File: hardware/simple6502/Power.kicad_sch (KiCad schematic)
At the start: 23 parts, among them J5 POWER 5V, J6 AUX 5VDC, SW2 POWER, U5 74HCT00, U6 74LS30, U7 74HCT273

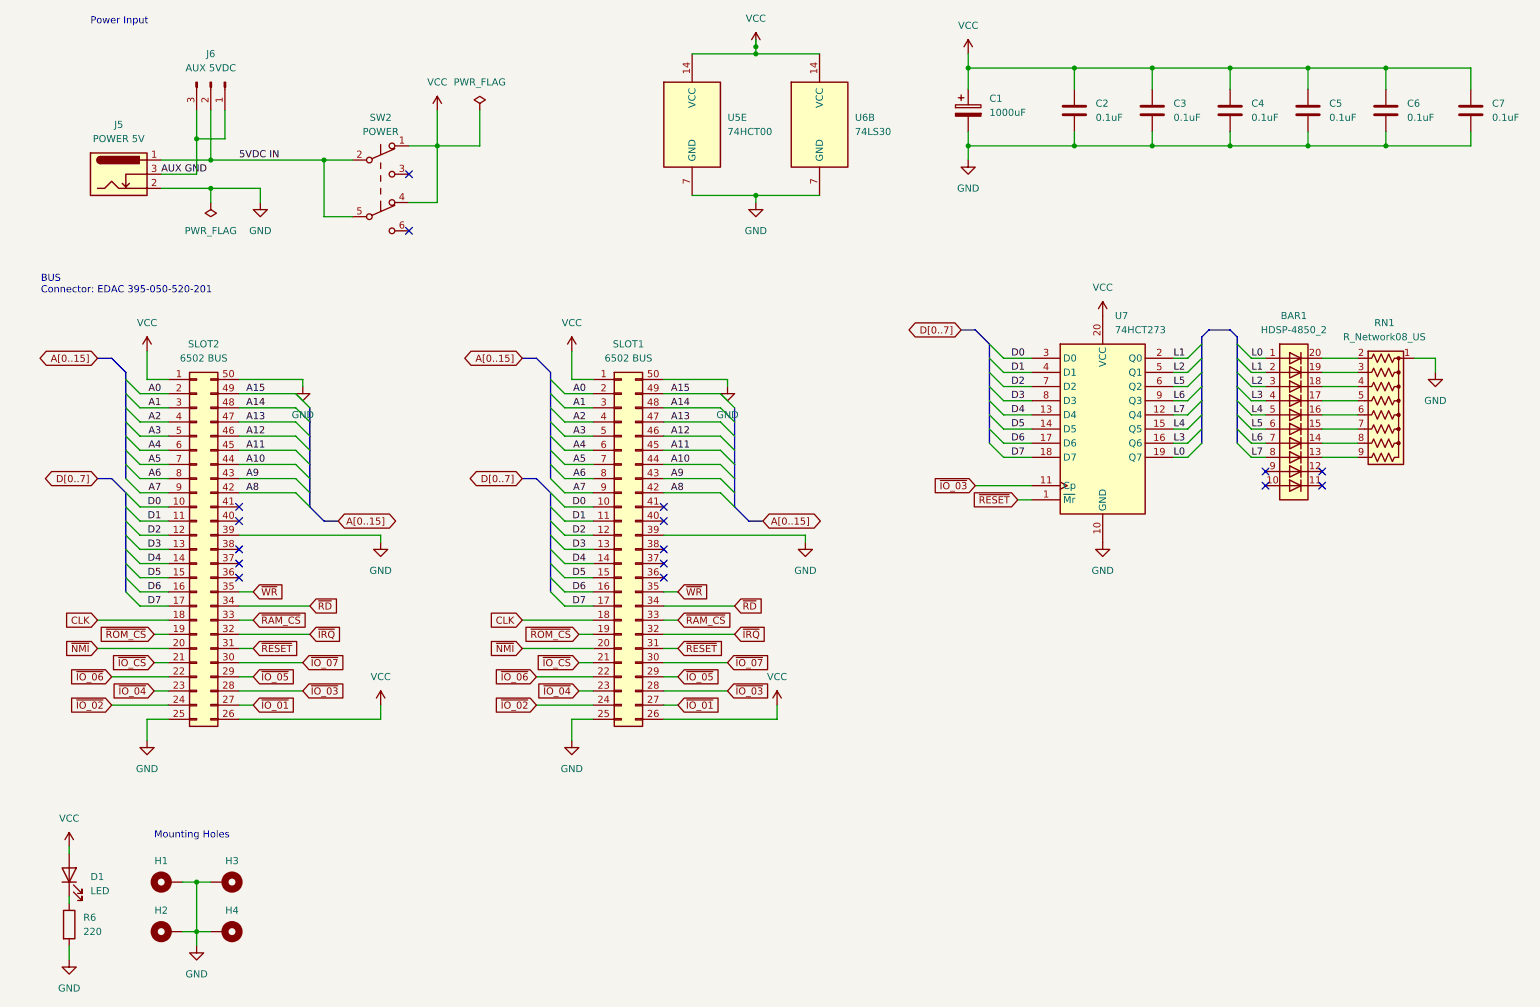
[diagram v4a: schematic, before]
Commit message: adding Debug leds in IO_8
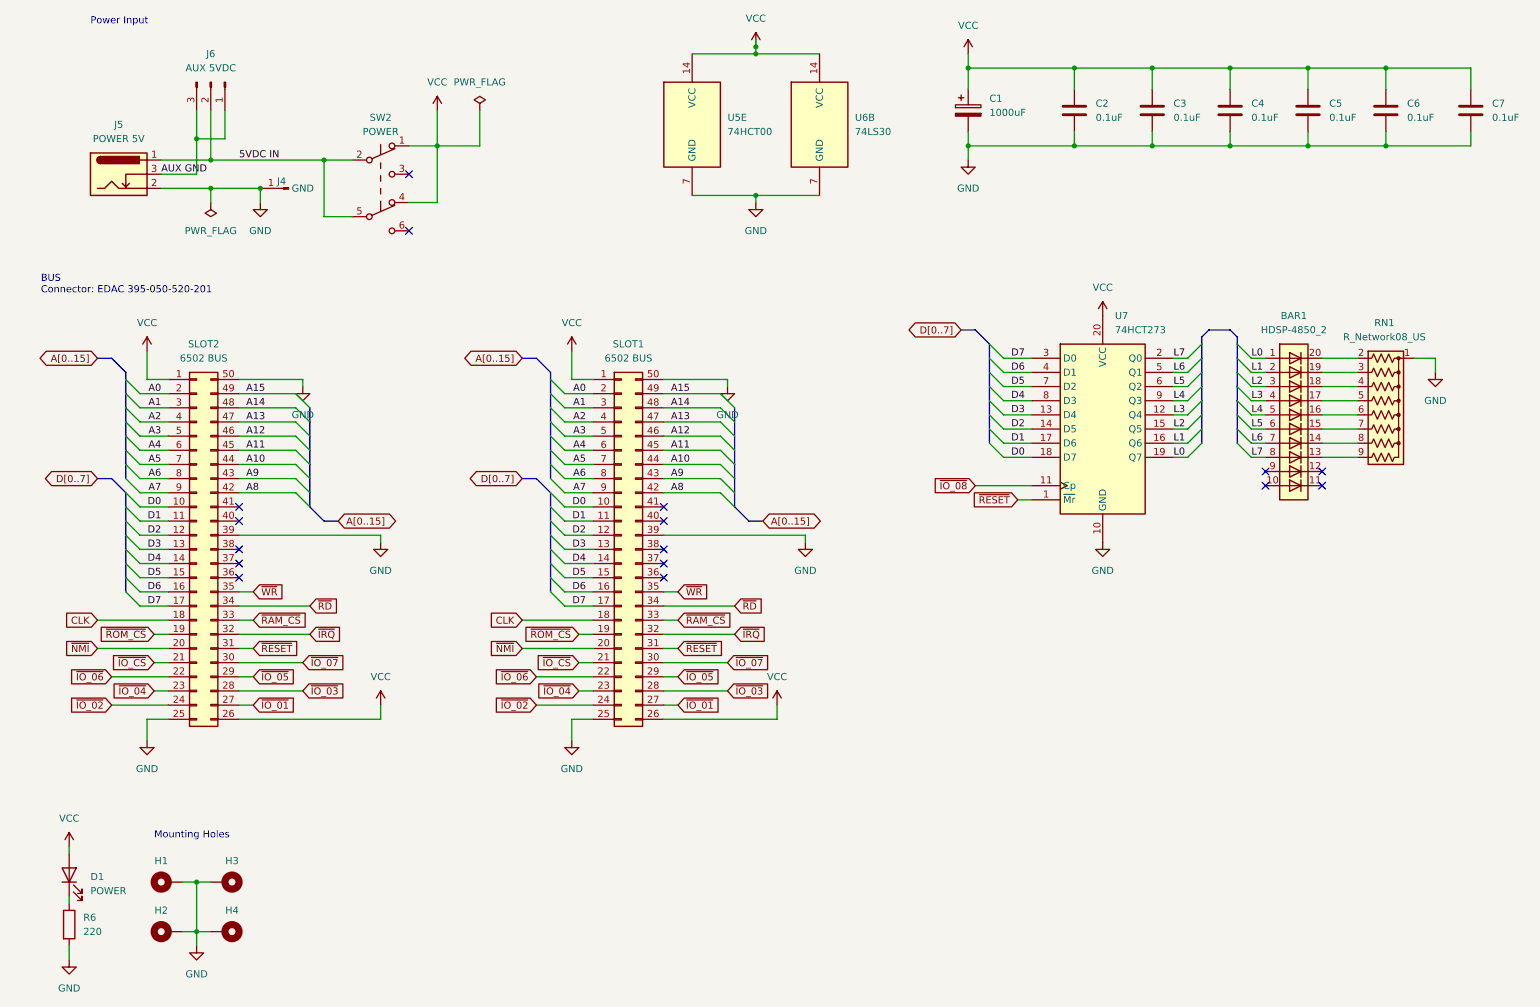
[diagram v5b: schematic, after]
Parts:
- added J4: GND, Connector_PinHeader_2.54mm:PinHeader_1x01_P2.54mm_Vertical, symbol Connector:Conn_01x01_Pin
- D1: value LED -> POWER
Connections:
- net D0: now also U7.18 (D7); no longer U7.3 (D0)
- net D1: now also U7.17 (D6); no longer U7.4 (D1)
- net D2: now also U7.14 (D5); no longer U7.7 (D2)
- net D3: now also U7.13 (D4); no longer U7.8 (D3)
- net D4: now also U7.8 (D3); no longer U7.13 (D4)
- net D5: now also U7.7 (D2); no longer U7.14 (D5)
- net D6: now also U7.4 (D1); no longer U7.17 (D6)
- net D7: now also U7.3 (D0); no longer U7.18 (D7)
- net GND: now also J4.1 (Pin_1)
- net L1: now also U7.16 (Q6); no longer U7.2 (Q0)
- net L2: now also U7.15 (Q5); no longer U7.5 (Q1)
- net L3: now also U7.12 (Q4); no longer U7.16 (Q6)
- net L4: now also U7.9 (Q3); no longer U7.15 (Q5)
- net L6: now also U7.5 (Q1); no longer U7.9 (Q3)
- net L7: now also U7.2 (Q0); no longer U7.12 (Q4)
- net ~{IO_03}: no longer U7.11 (Cp)
- new net ~{IO_08}: U7.11 (Cp)
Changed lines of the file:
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@@
   (title_block
     (title "simple6502")
-    (date "2023-09-25")
-    (rev "1.0")
+    (date "2023-10-01")
+    (rev "1.1")
     (company "Mariano Luna")
   )
@@
   )
   (junction (at 67.31 45.72) (diameter 0) (color 0 0 0 0)
+  )
+  (junction (at 55.88 50.8) (diameter 0) (color 0 0 0 0)
   )
   (junction (at 144.78 26.67) (diameter 0) (color 0 0 0 0)
@@
     (effects (font (size 1.27 1.27)) (justify left bottom))
   )
-  (label "L6" (at 219.71 88.9 0) (fields_autoplaced)
+  (label "L4" (at 219.71 88.9 0) (fields_autoplaced)
     (effects (font (size 1.27 1.27)) (justify left bottom))
   )
@@
     (effects (font (size 1.27 1.27)) (justify right bottom))
   )
-  (label "L4" (at 219.71 93.98 0) (fields_autoplaced)
+  (label "L2" (at 219.71 93.98 0) (fields_autoplaced)
     (effects (font (size 1.27 1.27)) (justify left bottom))
   )
@@
     (effects (font (size 1.27 1.27)) (justify left bottom))
   )
-  (label "D3" (at 193.04 88.9 180) (fields_autoplaced)
+  (label "D4" (at 193.04 88.9 180) (fields_autoplaced)
     (effects (font (size 1.27 1.27)) (justify right bottom))
   )
@@
     (effects (font (size 1.27 1.27)) (justify left bottom))
   )
-  (label "D5" (at 193.04 93.98 180) (fields_autoplaced)
-    (effects (font (size 1.27 1.27)) (justify right bottom))
-  )
-  (label "D6" (at 193.04 96.52 180) (fields_autoplaced)
+  (label "D2" (at 193.04 93.98 180) (fields_autoplaced)
+    (effects (font (size 1.27 1.27)) (justify right bottom))
+  )
+  (label "D1" (at 193.04 96.52 180) (fields_autoplaced)
     (effects (font (size 1.27 1.27)) (justify right bottom))
   )
@@
     (effects (font (size 1.27 1.27)) (justify right bottom))
   )
-  (label "D2" (at 193.04 86.36 180) (fields_autoplaced)
+  (label "D5" (at 193.04 86.36 180) (fields_autoplaced)
     (effects (font (size 1.27 1.27)) (justify right bottom))
   )
@@
     (effects (font (size 1.27 1.27)) (justify right bottom))
   )
-  (label "D7" (at 193.04 99.06 180) (fields_autoplaced)
+  (label "D0" (at 193.04 99.06 180) (fields_autoplaced)
     (effects (font (size 1.27 1.27)) (justify right bottom))
   )
@@
     (effects (font (size 1.27 1.27)) (justify left bottom))
   )
-  (label "D4" (at 193.04 91.44 180) (fields_autoplaced)
+  (label "D3" (at 193.04 91.44 180) (fields_autoplaced)
     (effects (font (size 1.27 1.27)) (justify right bottom))
   )
@@
     (effects (font (size 1.27 1.27)) (justify left bottom))
   )
-  (label "L1" (at 219.71 81.28 0) (fields_autoplaced)
+  (label "L7" (at 219.71 81.28 0) (fields_autoplaced)
     (effects (font (size 1.27 1.27)) (justify left bottom))
   )
@@
     (effects (font (size 1.27 1.27)) (justify right bottom))
   )
-  (label "L3" (at 219.71 96.52 0) (fields_autoplaced)
-    (effects (font (size 1.27 1.27)) (justify left bottom))
-  )
-  (label "D1" (at 193.04 83.82 180) (fields_autoplaced)
+  (label "L1" (at 219.71 96.52 0) (fields_autoplaced)
+    (effects (font (size 1.27 1.27)) (justify left bottom))
+  )
+  (label "D6" (at 193.04 83.82 180) (fields_autoplaced)
     (effects (font (size 1.27 1.27)) (justify right bottom))
   )
@@
     (effects (font (size 1.27 1.27)) (justify right bottom))
   )
-  (label "D0" (at 193.04 81.28 180) (fields_autoplaced)
+  (label "D7" (at 193.04 81.28 180) (fields_autoplaced)
     (effects (font (size 1.27 1.27)) (justify right bottom))
   )
@@
     (effects (font (size 1.27 1.27)) (justify right bottom))
   )
-  (label "L7" (at 219.71 91.44 0) (fields_autoplaced)
+  (label "L3" (at 219.71 91.44 0) (fields_autoplaced)
     (effects (font (size 1.27 1.27)) (justify left bottom))
   )
@@
     (effects (font (size 1.27 1.27)) (justify right bottom))
   )
-  (label "L2" (at 219.71 83.82 0) (fields_autoplaced)
+  (label "L6" (at 219.71 83.82 0) (fields_autoplaced)
     (effects (font (size 1.27 1.27)) (justify left bottom))
   )
@@
     )
   )
-  (global_label "~{IO_03}" (shape input) (at 184.15 104.14 180) (fields_autoplaced)
+  (global_label "~{IO_08}" (shape input) (at 184.15 104.14 180) (fields_autoplaced)
     (effects (font (size 1.27 1.27)) (justify right))
     (property "Intersheetrefs" "${INTERSHEET_REFS}" (at 175.8429 104.14 0)
@@
         (path "/c0007eb4-077e-4f77-aad9-8dd15548af06/710f29f6-117a-4dcb-a5e3-826b377de52e"
           (reference "#PWR040") (unit 1)
+        )
+      )
+    )
+  )
+  (symbol (lib_id "Connector:Conn_01x01_Pin") (at 60.96 50.8 180) (unit 1)
+    (in_bom yes) (on_board yes) (dnp no)
+    (property "Reference" "J4" (at 59.69 49.53 0)
+      (effects (font (size 1.27 1.27)))
+    )
+    (property "Value" "GND" (at 63.5 50.8 0)
+      (effects (font (size 1.27 1.27)))
+    )
+    (property "Footprint" "Connector_PinHeader_2.54mm:PinHeader_1x01_P2.54mm_Vertical" (at 60.96 50.8 0)
+      (effects (font (size 1.27 1.27)) hide)
+    )
+    (property "Datasheet" "~" (at 60.96 50.8 0)
+      (effects (font (size 1.27 1.27)) hide)
+    )
+    (pin "1")
+    (instances
+      (project "simple6502"
+        (path "/c0007eb4-077e-4f77-aad9-8dd15548af06/710f29f6-117a-4dcb-a5e3-826b377de52e"
+          (reference "J4") (unit 1)
         )
       )
@@
       (effects (font (size 1.27 1.27)) (justify right))
     )
-    (property "Value" "LED" (at 25.4 176.8475 90)
+    (property "Value" "POWER" (at 25.4 176.8475 90)
       (effects (font (size 1.27 1.27)) (justify right))
     )

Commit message: clean pcb board style
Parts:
- removed SLOT1: 6502 BUS, Connector_Card:EDAC 395-050-520-201, symbol Connector_Generic:Conn_02x25_Counter_Clockwise
- SLOT2: footprint Connector_Card:EDAC 395-050-520-201 -> Connector_PCBEdge:BUS_EdgePCB_Apple_2
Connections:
- net A0: now also SLOT2.6 (Pin_6); no longer SLOT2.2 (Pin_2)
- net A1: now also SLOT2.7 (Pin_7); no longer SLOT2.3 (Pin_3)
- net A10: now also SLOT2.40 (Pin_40); no longer SLOT2.44 (Pin_44)
- net A11: now also SLOT2.41 (Pin_41); no longer SLOT2.45 (Pin_45)
- net A12: now also SLOT2.42 (Pin_42); no longer SLOT2.46 (Pin_46)
- net A13: now also SLOT2.43 (Pin_43); no longer SLOT2.47 (Pin_47)
- net A14: now also SLOT2.44 (Pin_44); no longer SLOT2.48 (Pin_48)
- net A15: now also SLOT2.45 (Pin_45); no longer SLOT2.49 (Pin_49)
- net A2: now also SLOT2.8 (Pin_8); no longer SLOT2.4 (Pin_4)
- net A3: now also SLOT2.9 (Pin_9); no longer SLOT2.5 (Pin_5)
- net A4: now also SLOT2.10 (Pin_10); no longer SLOT2.6 (Pin_6)
- net A5: now also SLOT2.11 (Pin_11); no longer SLOT2.7 (Pin_7)
- net A6: now also SLOT2.12 (Pin_12); no longer SLOT2.8 (Pin_8)
- net A7: now also SLOT2.13 (Pin_13); no longer SLOT2.9 (Pin_9)
- net A8: now also SLOT2.38 (Pin_38); no longer SLOT2.42 (Pin_42)
- net A9: now also SLOT2.39 (Pin_39); no longer SLOT2.43 (Pin_43)
- net D0: now also SLOT2.46 (Pin_46); no longer SLOT2.10 (Pin_10)
- net D1: now also SLOT2.47 (Pin_47); no longer SLOT2.11 (Pin_11)
- net D2: now also SLOT2.48 (Pin_48); no longer SLOT2.12 (Pin_12)
- net D3: now also SLOT2.49 (Pin_49); no longer SLOT2.13 (Pin_13)
- net D4: now also SLOT2.2 (Pin_2); no longer SLOT2.14 (Pin_14)
- net D5: now also SLOT2.3 (Pin_3); no longer SLOT2.15 (Pin_15)
- net D6: now also SLOT2.4 (Pin_4); no longer SLOT2.16 (Pin_16)
- net D7: now also SLOT2.5 (Pin_5); no longer SLOT2.17 (Pin_17)
- net GND: no longer SLOT2.39 (Pin_39)
- no-connect marks 16 -> 6

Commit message: cpu board only ready
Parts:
- removed BAR1: HDSP-4850_2, Display:HDSP-4850, symbol LED:HDSP-4850_2
- removed C1: 1000uF, Capacitor_THT:CP_Radial_D6.3mm_P2.50mm, symbol Device:C_Polarized
- removed H1, H2, H3, H4: M, MountingHole:MountingHole_2.7mm_M2.5_Pad_Via, symbol Mechanical:MountingHole_Pad
- removed J4: GND, Connector_PinHeader_2.54mm:PinHeader_1x01_P2.54mm_Vertical, symbol Connector:Conn_01x01_Pin
- removed J5: POWER 5V, Connector_BarrelJack:BarrelJack_Horizontal, symbol Connector:Barrel_Jack_Switch
- removed RN1: R_Network08_US, Resistor_THT:R_Array_SIP9, symbol Device:R_Network08_US
- removed SW2: POWER, Button_Switch_THT:SW_Push_2P2T_Toggle_CK_PVA2OAH5xxxxxxV2, symbol Switch:SW_Push_DPDT
- removed U7: 74HCT273, Package_DIP:DIP-20_W7.62mm_Socket, symbol 74xx:74HCT273
- R6: value 220 -> 330
- renumbered C7 to C1
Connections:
- net 5VDC IN is gone; now on net VCC: J6.2 (Pin_2)
- net AUX GND is gone; now on net GND: J6.1 (Pin_1), J6.3 (Pin_3)
- net D0: now also SLOT2.5 (Pin_5); no longer SLOT2.46 (Pin_46)
- net D1: now also SLOT2.4 (Pin_4); no longer SLOT2.47 (Pin_47)
- net D2: now also SLOT2.3 (Pin_3); no longer SLOT2.48 (Pin_48)
- net D3: now also SLOT2.2 (Pin_2); no longer SLOT2.49 (Pin_49)
- net D4: now also SLOT2.49 (Pin_49); no longer SLOT2.2 (Pin_2)
- net D5: now also SLOT2.48 (Pin_48); no longer SLOT2.3 (Pin_3)
- net D6: now also SLOT2.47 (Pin_47); no longer SLOT2.4 (Pin_4)
- net D7: now also SLOT2.46 (Pin_46); no longer SLOT2.5 (Pin_5)
- net ~{IO_08}: now also SLOT2.21 (Pin_21)
- net ~{IO_CS}: now also SLOT2.20 (Pin_20); no longer SLOT2.21 (Pin_21)
- net ~{NMI}: now also SLOT2.19 (Pin_19); no longer SLOT2.20 (Pin_20)
- net ~{RAM_CS}: now also SLOT2.36 (Pin_36); no longer SLOT2.33 (Pin_33)
- net ~{RD}: now also SLOT2.16 (Pin_16); no longer SLOT2.34 (Pin_34)
- net ~{ROM_CS}: now also SLOT2.17 (Pin_17); no longer SLOT2.19 (Pin_19)
- no-connect marks 6 -> 5
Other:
- note removed: "Mounting Holes"
- moved on the sheet: C1, C2, C3, C4, C5, C6, D1, J6, R6, SLOT2

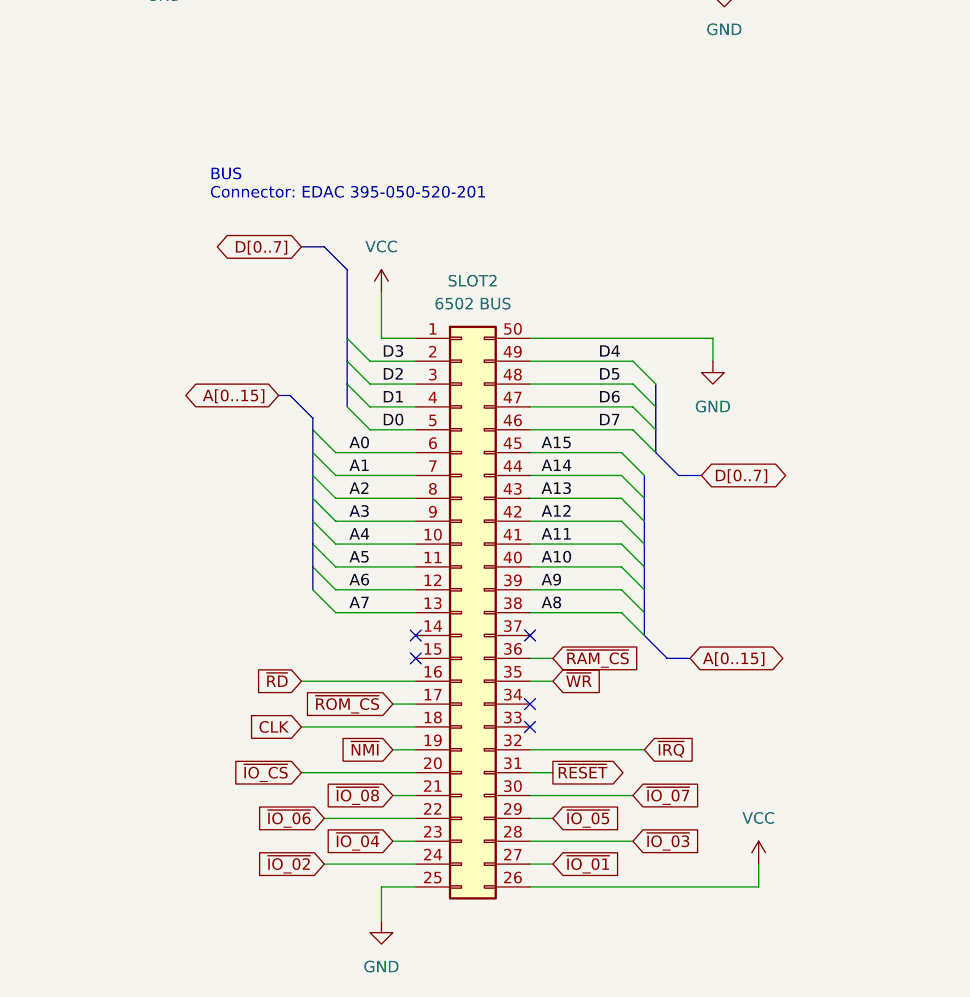
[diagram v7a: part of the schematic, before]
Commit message: adding schematic pdf and board images
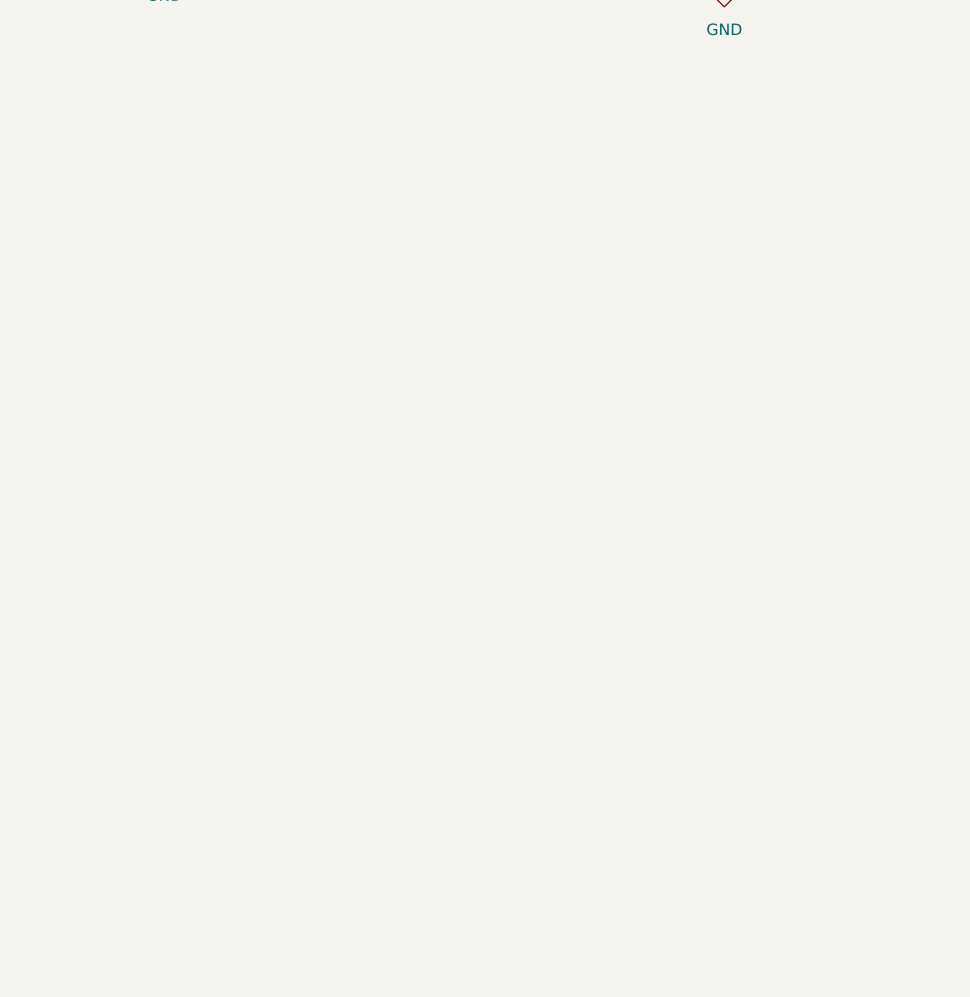
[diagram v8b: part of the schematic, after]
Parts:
- removed SLOT2: 6502 BUS, Connector_PCBEdge:BUS_EdgePCB_Apple_2, symbol Connector_Generic:Conn_02x25_Counter_Clockwise
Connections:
- no-connect marks 5 -> 0
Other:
- note removed: "BUS Connector: EDAC 395-050-520-201"
